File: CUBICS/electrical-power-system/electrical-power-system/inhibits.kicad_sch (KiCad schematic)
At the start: 10 parts, among them Q1 CSD17578Q3A, SW1 SW_Push_SPDT, SW2 SW_Push_SPDT, SW3 SW_Push_SPDT, SW4 SW_Push_SPDT, SW5 SW_Push_SPDT, SW6 SW_Push_SPDT, SW7 SW_Push_SPDT

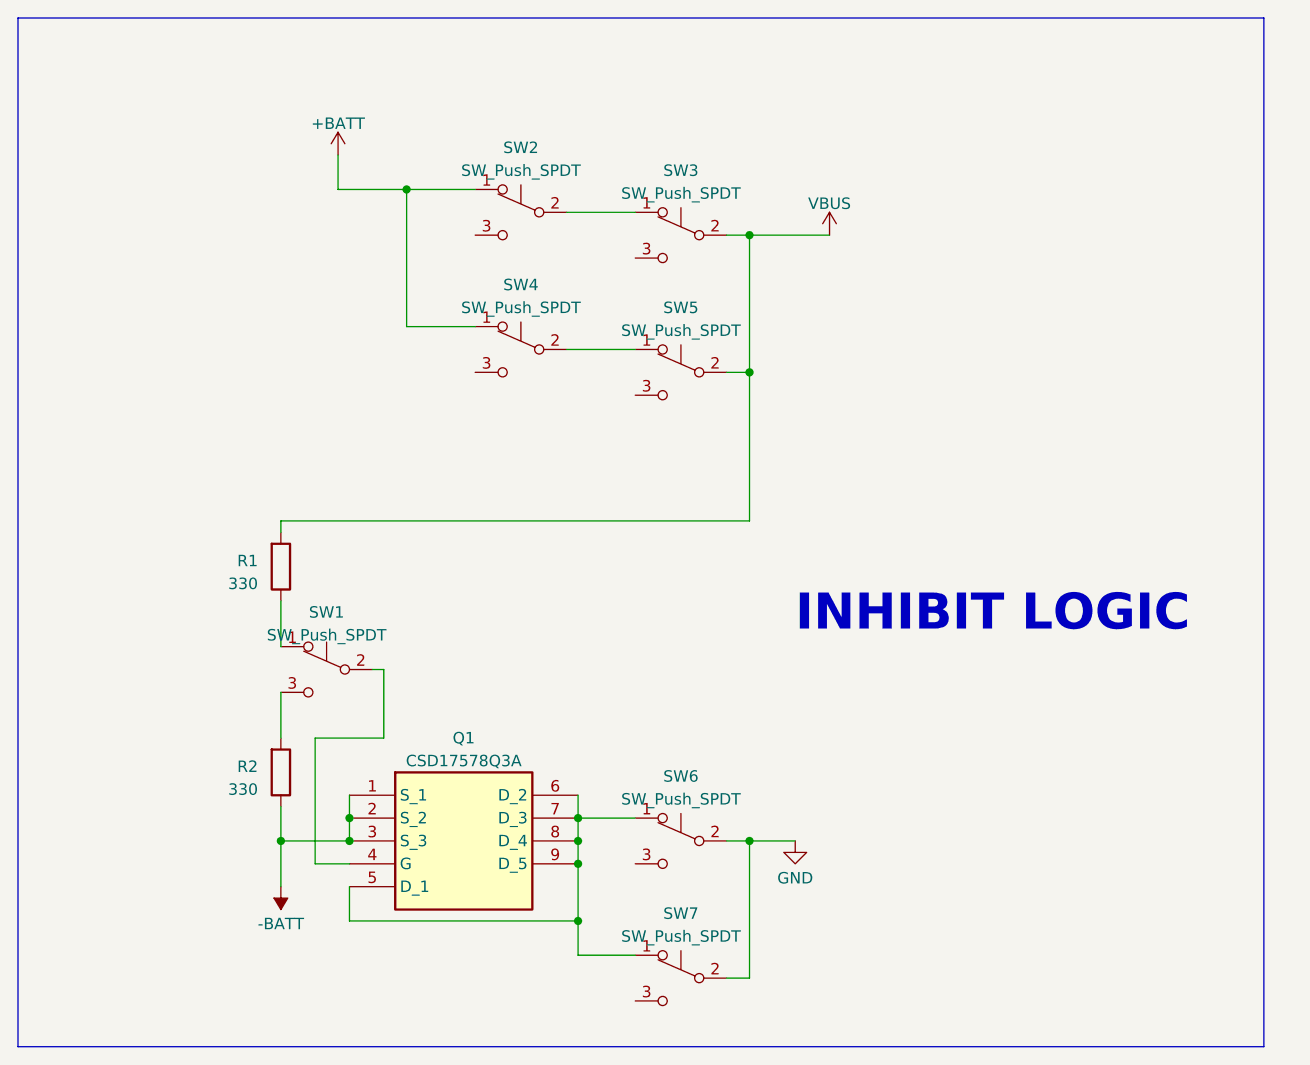
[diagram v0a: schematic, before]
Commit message: rev 1.0 routing complete updated schematic
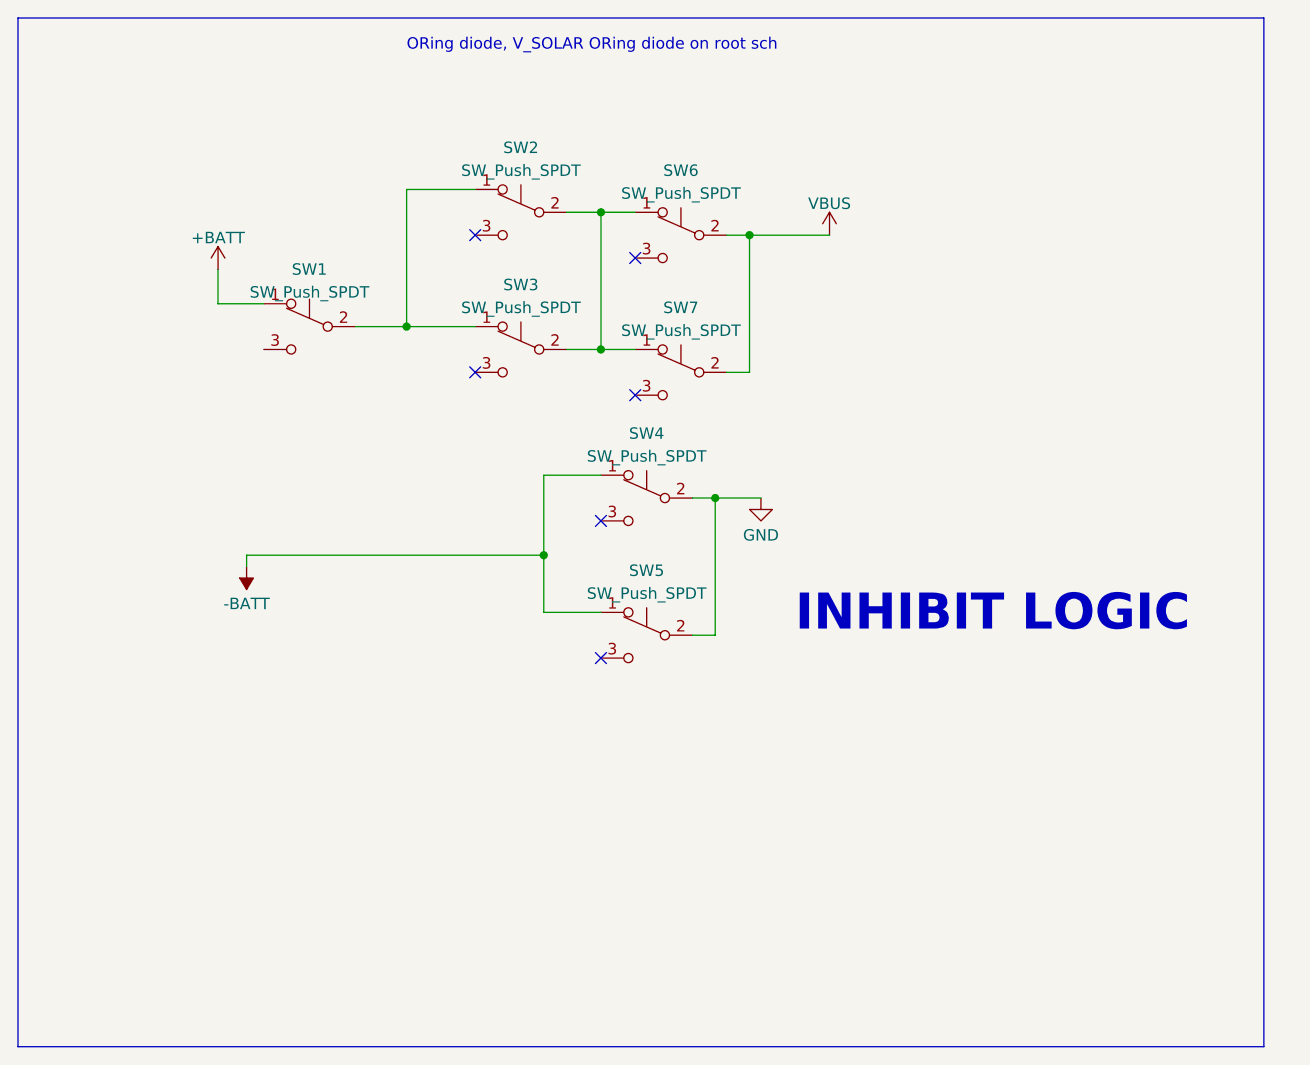
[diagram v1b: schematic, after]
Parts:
- removed Q1: CSD17578Q3A, SamacSys_Parts:Q3A, symbol SamacSys_Parts:CSD17578Q3A
- removed R1, R2: 330, Resistor_SMD:R_0603_1608Metric, symbol Device:R
- renumbered SW4 to SW3, SW6 to SW4, SW7 to SW5, SW3 to SW6, SW5 to SW7
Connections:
- net +BATT: now also SW1.1 (A); no longer SW2.1 (A), SW3.1 (A)
- net -BATT: now also SW4.1 (A), SW5.1 (A)
- net at SW2.2 (B), SW6.1 (A): now also SW3.2 (B), SW7.1 (A)
- net at SW1.2 (B): now also SW2.1 (A), SW3.1 (A)
- no-connect marks 0 -> 6
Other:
- note added: "ORing diode, V_SOLAR ORing diode on root sch"
- moved on the sheet: SW1, SW4, SW5
